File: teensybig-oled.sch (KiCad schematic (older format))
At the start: 3 parts, among them J1 TEENSY-LC, J2 OLED-I2C

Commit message: uploaded to oshpark
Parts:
- removed J2: OLED-I2C, Wickerlib:Pin_Header_Straight_1x06, symbol HEADER-FEMALE-6POS-TH-1x06-P0.1IN
- removed J?: ADAFRUIT_BME280, CONN-1x07-2.54MM-TH, symbol HEADER-FEMALE-7POS-TH-1x07-P0.1IN
- added J2: OLED_128x64, Wickerlib:Pin_Header_Straight_1x08, symbol HEADER-FEMALE-8POS-TH-1x08-P0.1IN
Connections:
- net labels added: 3V3, CLK, DC, Data, MOSI, SA0/DC
- net labels removed: 3.3V, 3V0, SCK, SCL, SDA, SDI, SDO
- wire segments 30 -> 29
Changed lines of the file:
@@
 LIBS:valves
 LIBS:wickerlib
-LIBS:teensyi2c-cache
+LIBS:teensybig-oled-cache
 EELAYER 25 0
 EELAYER END
@@
 	1    0    0    -1
 $EndComp
+Text Label 6000 2725 0    60   ~ 0
+CS
+Text Label 6025 2825 0    60   ~ 0
+RST
+Text Label 6225 2925 0    60   ~ 0
+DC
+Text Label 5500 3350 0    60   ~ 0
+CLK
+Text Label 5500 3250 0    60   ~ 0
+MOSI
 Text Label 5925 2150 0    60   ~ 0
 VIN
 $Comp
-L HEADER-FEMALE-6POS-TH-1x06-P0.1IN J2
-U 1 1 57712F77
-P 7550 3475
-F 0 "J2" H 7550 3925 50  0000 L CNN
-F 1 "OLED-I2C" H 7550 3825 50  0000 L CNN
-F 2 "Wickerlib:Pin_Header_Straight_1x06" H 7550 3125 50  0001 C CIN
-F 3 "https://cdn.harwin.com/pdfs/60page140.pdf" H 7550 3475 5   0001 C CNN
-F 4 "Pin_Header_Straight_1x06" H 7550 3125 50  0001 C CIN "Package"
-F 5 "Harwin" H 7550 3125 50  0001 C CIN "MF_Name"
-F 6 "M20-7820642" H 7550 3125 50  0001 C CIN "MF_PN"
-F 7 "Digikey" H 7550 3125 50  0001 C CIN "S1_Name"
-F 8 "952-1808-ND" H 7550 3125 50  0001 C CIN "S1_PN"
-F 9 "HEADER FEMALE 6POS TH 1x06 0.1”" H 7550 3125 50  0001 C CIN "Description"
-F 10 "Not Verified" H 7550 3125 50  0001 C CIN "Verified"
-	1    7550 3475
+L HEADER-FEMALE-8POS-TH-1x08-P0.1IN J2
+U 1 1 573AD5FE
+P 7625 3150
+F 0 "J2" H 7625 3600 50  0000 L CNN
+F 1 "OLED_128x64" H 7625 3500 50  0000 L CNN
+F 2 "Wickerlib:Pin_Header_Straight_1x08" H 7625 2800 50  0001 C CIN
+F 3 "https://cdn.harwin.com/pdfs/60page140.pdf" H 7625 3150 5   0001 C CNN
+F 4 "Pin_Header_Straight_1x08" H 7625 2800 50  0001 C CIN "Package"
+F 5 "Harwin" H 7625 2800 50  0001 C CIN "MF_Name"
+F 6 "M20-7820842" H 7625 2800 50  0001 C CIN "MF_PN"
+F 7 "Digikey" H 7625 2800 50  0001 C CIN "S1_Name"
+F 8 "952-1823-ND" H 7625 2800 50  0001 C CIN "S1_PN"
+F 9 "HEADER FEMALE 8POS TH 1x08 0.1”" H 7625 2800 50  0001 C CIN "Description"
+F 10 "Not Verified" H 7625 2800 50  0001 C CIN "Verified"
+	1    7625 3150
 	1    0    0    -1
 $EndComp
-Wire Wire Line
-	5525 2150 8200 2150
-Wire Wire Line
-	5825 3225 7350 3225
-Wire Wire Line
-	5975 3325 7350 3325
-Wire Wire Line
-	6150 3425 7350 3425
-Wire Wire Line
-	6775 3525 7350 3525
-Wire Wire Line
-	7350 3625 6950 3625
-Wire Wire Line
-	7350 3725 6900 3725
-Text Label 7150 3225 0    60   ~ 0
-SDA
-Text Label 7150 3325 0    60   ~ 0
-SCL
-Text Label 7150 3425 0    60   ~ 0
+Text Label 7250 2800 0    60   ~ 0
+GND
+Text Label 7275 2900 0    60   ~ 0
+VIN
+Text Label 7250 3000 0    60   ~ 0
+3V3
+Text Label 7250 3100 0    60   ~ 0
+CS
+Text Label 7250 3200 0    60   ~ 0
 RST
-Text Label 7150 3525 0    60   ~ 0
-GND
-Text Label 7150 3625 0    60   ~ 0
-3.3V
-Text Label 7175 3725 0    60   ~ 0
-VIN
-Wire Wire Line
-	5825 3225 5825 4150
-Wire Wire Line
-	5825 4150 5475 4150
-Wire Wire Line
-	5975 3325 5975 4250
-Wire Wire Line
-	5975 4250 5475 4250
-Wire Wire Line
-	6150 3425 6150 2750
-Wire Wire Line
-	6150 2750 5475 2750
-Wire Wire Line
-	6775 3525 6775 5150
+Text Label 7050 3300 0    60   ~ 0
+SA0/DC
+Text Label 7225 3400 0    60   ~ 0
+CLK
+Text Label 7175 3500 0    60   ~ 0
+Data
 Text Label 5875 5150 0    60   ~ 0
 GND
+Text Label 5500 3550 0    60   ~ 0
+CS
+Text Label 5500 3650 0    60   ~ 0
+RST
+Text Label 5500 3450 0    60   ~ 0
+DC
 Wire Wire Line
-	5475 5150 8200 5150
+	5825 2725 7075 2725
 Wire Wire Line
-	6900 3725 6900 2150
-$Comp
-L HEADER-FEMALE-7POS-TH-1x07-P0.1IN J?
-U 1 1 57713409
-P 8725 3450
-F 0 "J?" H 8725 3900 50  0000 L CNN
-F 1 "ADAFRUIT_BME280" H 8725 3800 50  0000 L CNN
-F 2 "CONN-1x07-2.54MM-TH" H 8725 3100 50  0001 C CIN
-F 3 "https://cdn.harwin.com/pdfs/60page140.pdf" H 8725 3450 5   0001 C CNN
-F 4 "Pin_Header_Straight_1x07" H 8725 3100 50  0001 C CIN "Package"
-F 5 "Harwin" H 8725 3100 50  0001 C CIN "MF_Name"
-F 6 "M20-7822046" H 8725 3100 50  0001 C CIN "MF_PN"
-F 7 "Digikey" H 8725 3100 50  0001 C CIN "S1_Name"
-F 8 "952-1905-ND" H 8725 3100 50  0001 C CIN "S1_PN"
-F 9 "HEADER FEMALE 7POS TH 1x07 0.1”" H 8725 3100 50  0001 C CIN "Description"
-F 10 "Not Verified" H 8725 3100 50  0001 C CIN "Verified"
-	1    8725 3450
-	1    0    0    -1
-$EndComp
+	5825 2725 5825 3550
 Wire Wire Line
-	8525 3150 8200 3150
+	5825 3550 5475 3550
 Wire Wire Line
-	8200 3150 8200 2150
-Connection ~ 6900 2150
+	5975 2825 5975 3650
 Wire Wire Line
-	8525 3350 8200 3350
+	5975 3650 5475 3650
 Wire Wire Line
-	8200 3350 8200 5150
-Connection ~ 6775 5150
+	5475 3450 6100 3450
 Wire Wire Line
-	8525 3450 7725 3450
+	6100 3450 6100 2925
 Wire Wire Line
-	7725 3450 7725 3900
+	5475 3350 6700 3350
 Wire Wire Line
-	7725 3900 5975 3900
-Connection ~ 5975 3900
+	5475 3250 6775 3250
 Wire Wire Line
-	8525 3650 7775 3650
+	5525 2150 7125 2150
 Wire Wire Line
-	7775 3650 7775 4025
+	6700 3400 7425 3400
 Wire Wire Line
-	7775 4025 5825 4025
-Connection ~ 5825 4025
+	6975 2925 6975 3300
 Wire Wire Line
-	8525 3250 8200 3250
+	6100 2925 6975 2925
 Wire Wire Line
-	8300 3550 8525 3550
+	6775 3500 7425 3500
 Wire Wire Line
-	8525 3750 8300 3750
+	5475 5150 8375 5150
 Wire Wire Line
-	8300 3750 8300 3725
-Text Label 8350 3150 0    60   ~ 0
-VIN
-Text Label 8325 3250 0    60   ~ 0
-3V0
-Text Label 8300 3350 0    60   ~ 0
-GND
-Text Label 8325 3450 0    60   ~ 0
-SCK
-Text Label 8325 3550 0    60   ~ 0
-SDO
-Text Label 8350 3650 0    60   ~ 0
-SDI
-Text Label 8375 3750 0    60   ~ 0
-CS
+	8375 5150 8375 2425
+Wire Wire Line
+	8375 2425 7175 2425
+Wire Wire Line
+	7175 2425 7175 2800
+Wire Wire Line
+	7175 2800 7425 2800
+Wire Wire Line
+	7425 2900 7125 2900
+Wire Wire Line
+	7125 2900 7125 2150
+Wire Wire Line
+	7075 2725 7075 3100
+Wire Wire Line
+	7075 3100 7425 3100
+Wire Wire Line
+	6975 3300 7425 3300
+Wire Wire Line
+	7025 2825 7025 3200
+Wire Wire Line
+	7025 3200 7425 3200
+Wire Wire Line
+	6700 3350 6700 3400
+Wire Wire Line
+	5975 2825 7025 2825
+Wire Wire Line
+	6775 3250 6775 3500
 $EndSCHEMATC

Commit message: slim version
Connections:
- no-connect marks 0 -> 1
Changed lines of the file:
@@
 Wire Wire Line
 	6775 3250 6775 3500
+NoConn ~ 7425 3000
 $EndSCHEMATC

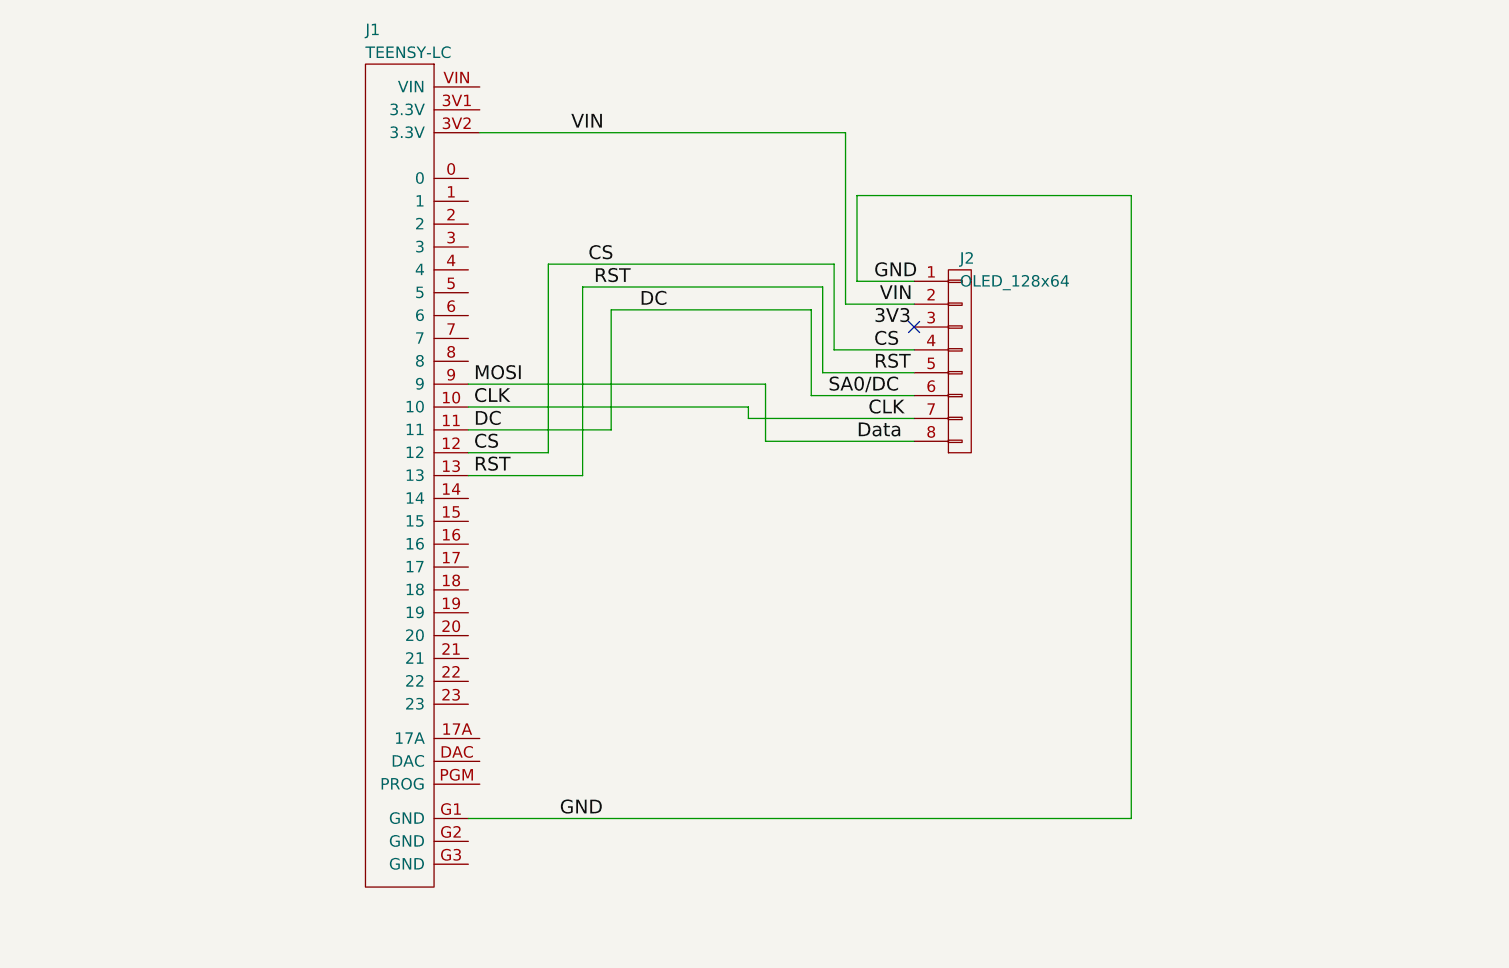
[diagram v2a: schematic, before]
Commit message: add cap touch buttons
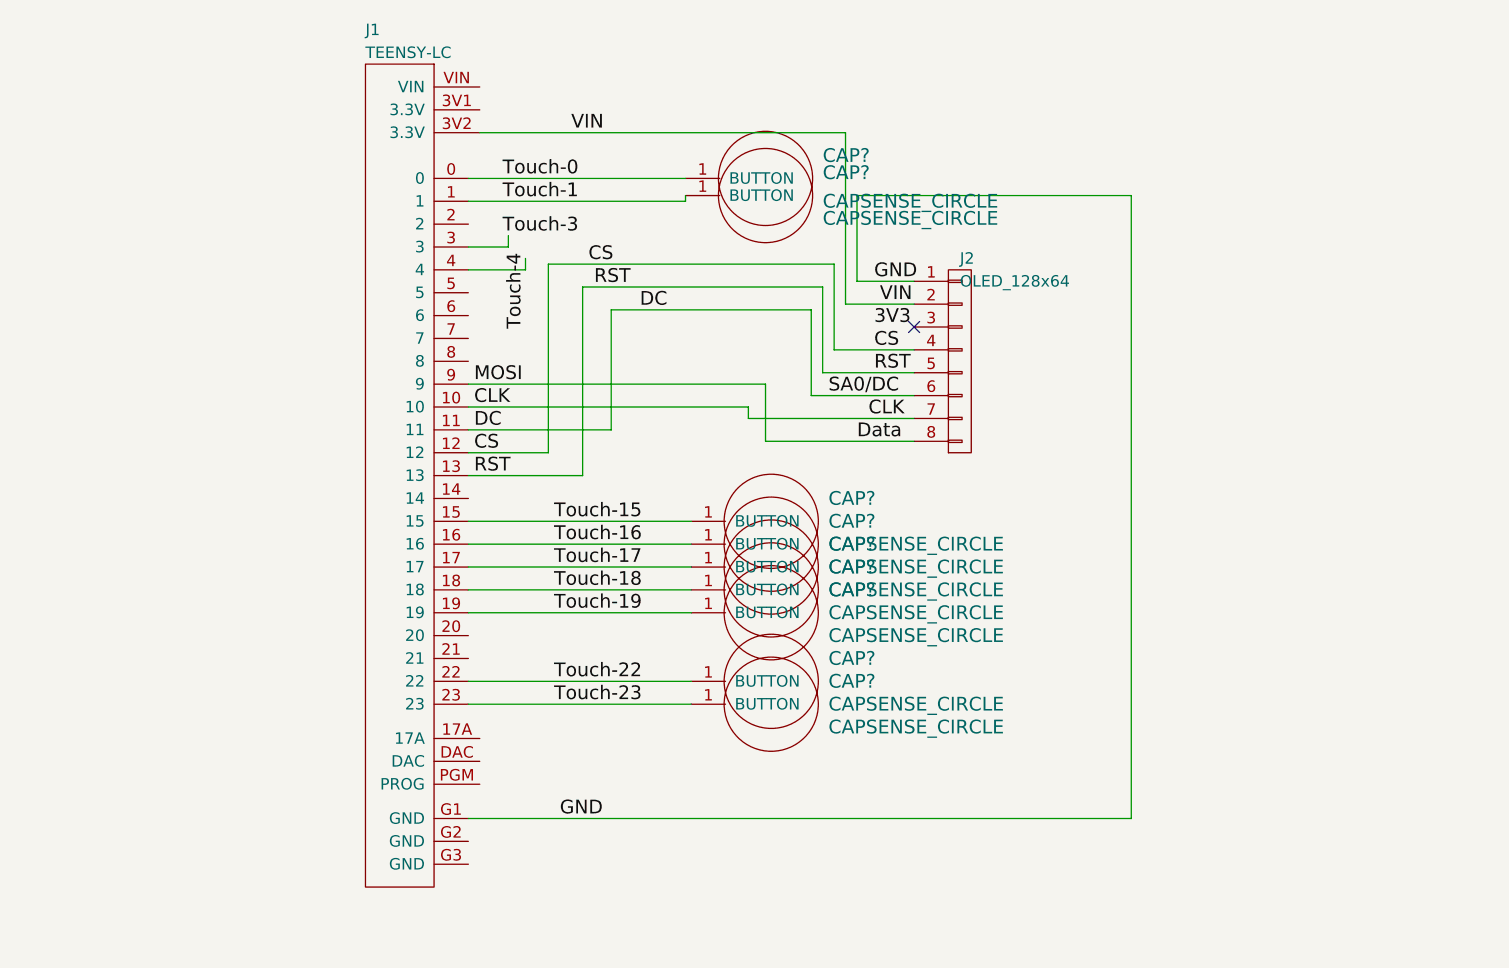
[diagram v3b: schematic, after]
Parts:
- added CAP? (x9): CAPSENSE_CIRCLE, symbol CAPSENSE_CIRCLE
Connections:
- net labels added: Touch-0, Touch-1, Touch-15, Touch-16, Touch-17, Touch-18, Touch-19, Touch-22, Touch-23, Touch-3, Touch-4
- wire segments 29 -> 43
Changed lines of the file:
@@
 Text Label 5500 3450 0    60   ~ 0
 DC
+NoConn ~ 7425 3000
+Text Label 5850 4250 0    60   ~ 0
+Touch-19
+Text Label 5850 4550 0    60   ~ 0
+Touch-22
+Text Label 5850 4650 0    60   ~ 0
+Touch-23
 Wire Wire Line
 	5825 2725 7075 2725
@@
 Wire Wire Line
 	6775 3250 6775 3500
-NoConn ~ 7425 3000
+Wire Wire Line
+	5475 4650 6450 4650
+Wire Wire Line
+	5475 4550 6450 4550
+Wire Wire Line
+	5475 4250 6450 4250
+Wire Wire Line
+	5475 4150 6450 4150
+Wire Wire Line
+	5475 4050 6450 4050
+Wire Wire Line
+	5475 3950 6450 3950
+Wire Wire Line
+	5475 3850 6450 3850
+Wire Wire Line
+	5475 2350 6425 2350
+Wire Wire Line
+	5475 2450 6425 2450
+Wire Wire Line
+	6425 2450 6425 2425
+Wire Wire Line
+	5475 2650 5650 2650
+Wire Wire Line
+	5650 2650 5650 2600
+Wire Wire Line
+	5475 2750 5725 2750
+Wire Wire Line
+	5725 2750 5725 2700
+Text Label 5625 2350 0    60   ~ 0
+Touch-0
+Text Label 5625 2450 0    60   ~ 0
+Touch-1
+Text Label 5625 2600 0    60   ~ 0
+Touch-3
+Text Label 5725 2675 3    60   ~ 0
+Touch-4
+Text Label 5850 4150 0    60   ~ 0
+Touch-18
+Text Label 5850 4050 0    60   ~ 0
+Touch-17
+Text Label 5850 3950 0    60   ~ 0
+Touch-16
+Text Label 5850 3850 0    60   ~ 0
+Touch-15
+$Comp
+L CAPSENSE_CIRCLE CAP?
+U 1 1 578C73B1
+P 6800 3850
+F 0 "CAP?" H 7050 3950 60  0000 L CNN
+F 1 "CAPSENSE_CIRCLE" H 7050 3750 60  0000 L CNN
+F 2 "" H 6800 3850 60  0000 C CNN
+F 3 "" H 6800 3850 60  0000 C CNN
+	1    6800 3850
+	1    0    0    -1
+$EndComp
+$Comp
+L CAPSENSE_CIRCLE CAP?
+U 1 1 578C744A
+P 6800 3950
+F 0 "CAP?" H 7050 4050 60  0000 L CNN
+F 1 "CAPSENSE_CIRCLE" H 7050 3850 60  0000 L CNN
+F 2 "" H 6800 3950 60  0000 C CNN
+F 3 "" H 6800 3950 60  0000 C CNN
+	1    6800 3950
+	1    0    0    -1
+$EndComp
+$Comp
+L CAPSENSE_CIRCLE CAP?
+U 1 1 578C750B
+P 6800 4050
+F 0 "CAP?" H 7050 4150 60  0000 L CNN
+F 1 "CAPSENSE_CIRCLE" H 7050 3950 60  0000 L CNN
+F 2 "" H 6800 4050 60  0000 C CNN
+F 3 "" H 6800 4050 60  0000 C CNN
+	1    6800 4050
+	1    0    0    -1
+$EndComp
+$Comp
+L CAPSENSE_CIRCLE CAP?
+U 1 1 578C755C
+P 6800 4150
+F 0 "CAP?" H 7050 4250 60  0000 L CNN
+F 1 "CAPSENSE_CIRCLE" H 7050 4050 60  0000 L CNN
+F 2 "" H 6800 4150 60  0000 C CNN
+F 3 "" H 6800 4150 60  0000 C CNN
+	1    6800 4150
+	1    0    0    -1
+$EndComp
+$Comp
+L CAPSENSE_CIRCLE CAP?
+U 1 1 578C75FB
+P 6800 4250
+F 0 "CAP?" H 7050 4350 60  0000 L CNN
+F 1 "CAPSENSE_CIRCLE" H 7050 4150 60  0000 L CNN
+F 2 "" H 6800 4250 60  0000 C CNN
+F 3 "" H 6800 4250 60  0000 C CNN
+	1    6800 4250
+	1    0    0    -1
+$EndComp
+$Comp
+L CAPSENSE_CIRCLE CAP?
+U 1 1 578C7694
+P 6800 4550
+F 0 "CAP?" H 7050 4650 60  0000 L CNN
+F 1 "CAPSENSE_CIRCLE" H 7050 4450 60  0000 L CNN
+F 2 "" H 6800 4550 60  0000 C CNN
+F 3 "" H 6800 4550 60  0000 C CNN
+	1    6800 4550
+	1    0    0    -1
+$EndComp
+$Comp
+L CAPSENSE_CIRCLE CAP?
+U 1 1 578C7721
+P 6800 4650
+F 0 "CAP?" H 7050 4750 60  0000 L CNN
+F 1 "CAPSENSE_CIRCLE" H 7050 4550 60  0000 L CNN
+F 2 "" H 6800 4650 60  0000 C CNN
+F 3 "" H 6800 4650 60  0000 C CNN
+	1    6800 4650
+	1    0    0    -1
+$EndComp
+$Comp
+L CAPSENSE_CIRCLE CAP?
+U 1 1 578C77CB
+P 6775 2350
+F 0 "CAP?" H 7025 2450 60  0000 L CNN
+F 1 "CAPSENSE_CIRCLE" H 7025 2250 60  0000 L CNN
+F 2 "" H 6775 2350 60  0000 C CNN
+F 3 "" H 6775 2350 60  0000 C CNN
+	1    6775 2350
+	1    0    0    -1
+$EndComp
+$Comp
+L CAPSENSE_CIRCLE CAP?
+U 1 1 578C789A
+P 6775 2425
+F 0 "CAP?" H 7025 2525 60  0000 L CNN
+F 1 "CAPSENSE_CIRCLE" H 7025 2325 60  0000 L CNN
+F 2 "" H 6775 2425 60  0000 C CNN
+F 3 "" H 6775 2425 60  0000 C CNN
+	1    6775 2425
+	1    0    0    -1
+$EndComp
 $EndSCHEMATC

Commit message: update schematic
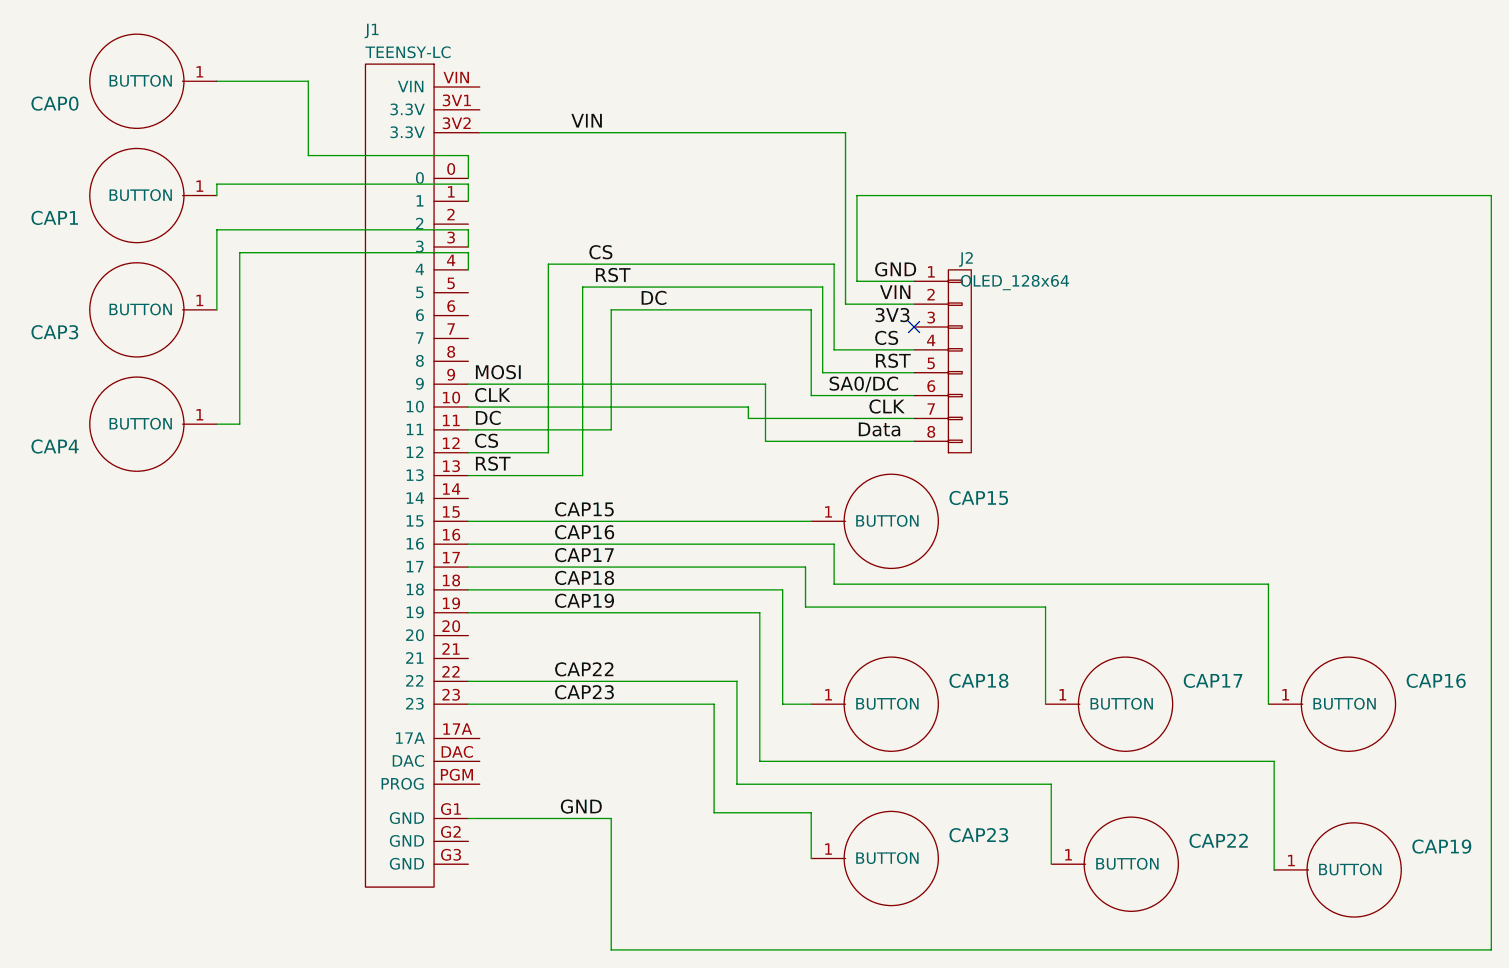
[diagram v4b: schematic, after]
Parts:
- removed CAP?: CAPSENSE_CIRCLE, symbol CAPSENSE_CIRCLE
- added CAP1, CAP3, CAP4: CAPSENSE_CIRCLE, Wickerlib:CAPSENSE_CIRCLE_D10, symbol CAPSENSE_CIRCLE
- CAP0, CAP15, CAP16, CAP17, CAP18, CAP19, CAP22, CAP23: renamed from CAP?; footprint (none) -> Wickerlib:CAPSENSE_CIRCLE_D10
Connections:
- net labels added: CAP15, CAP16, CAP17, CAP18, CAP19, CAP22, CAP23
- net labels removed: Touch-0, Touch-1, Touch-15, Touch-16, Touch-17, Touch-18, Touch-19, Touch-22, Touch-23, Touch-3, Touch-4
- wire segments 43 -> 69
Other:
- moved on the sheet: CAP0, CAP15, CAP16, CAP17, CAP18, CAP19, CAP22, CAP23
